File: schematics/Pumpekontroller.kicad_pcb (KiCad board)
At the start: 2 copper layers, 129.5 x 85.1 mm, 15 parts, among them Q1 BC548, Q2 BC548, SW1 SW_Push, SW2 SW_Push, U1 WeMos_D1_mini

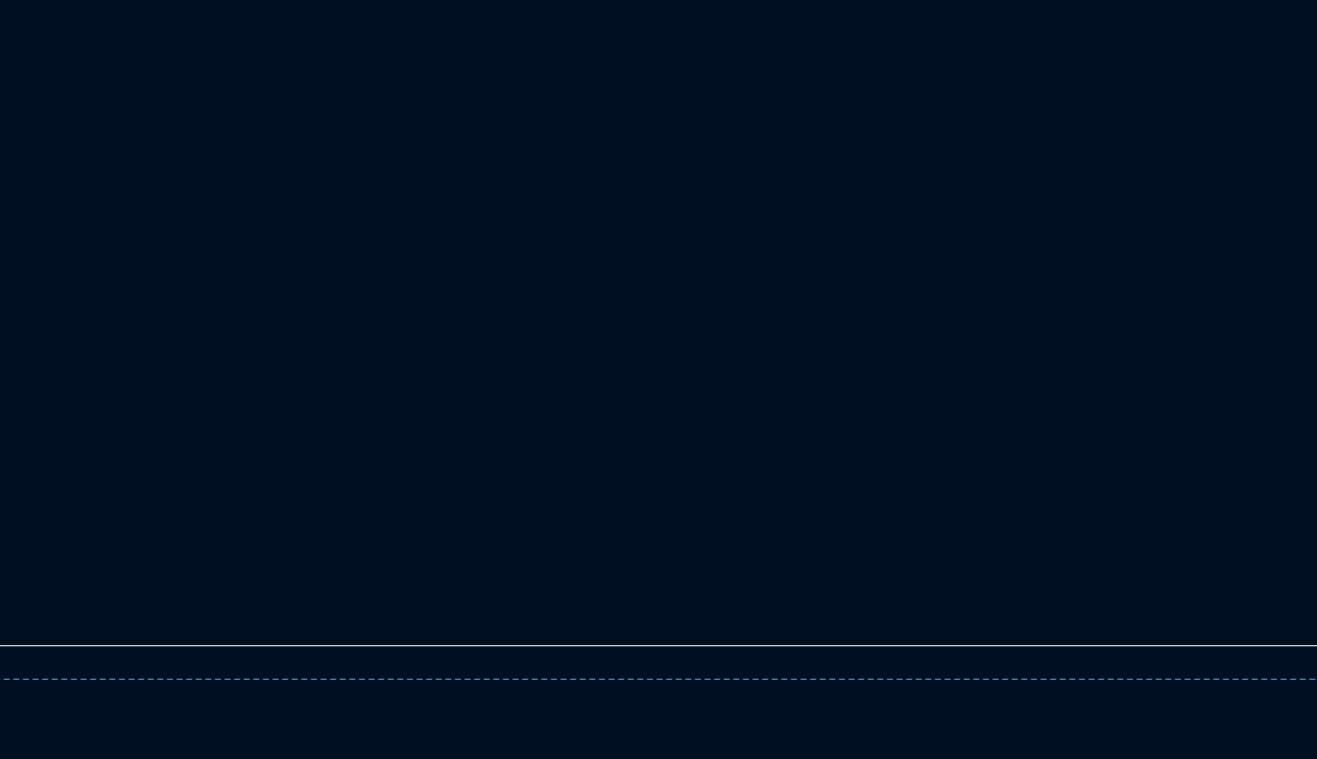
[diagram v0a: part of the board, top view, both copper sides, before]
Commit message: Update schematics with relay and pump circuit. Need more work.
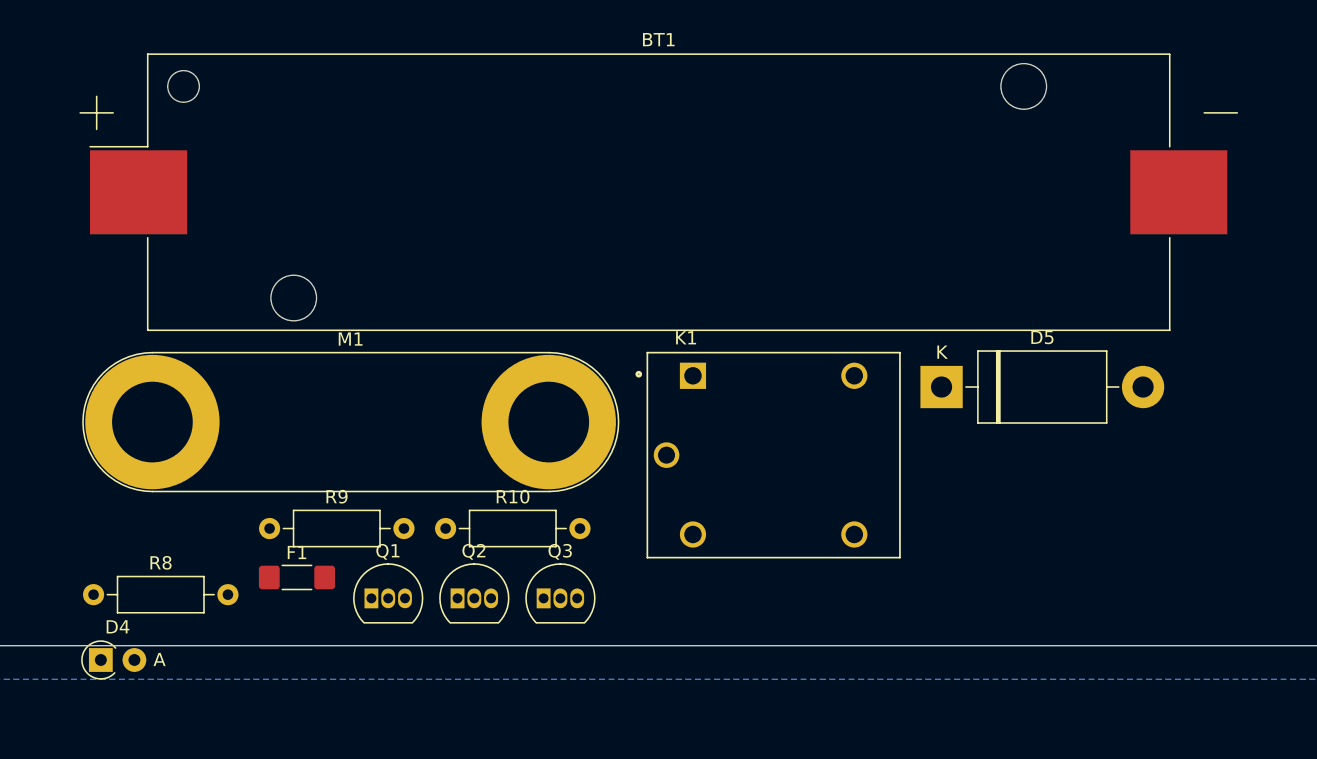
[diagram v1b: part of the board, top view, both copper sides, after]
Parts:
- added BT1: Battery 12V, Battery:BatteryHolder_Keystone_1042_1x18650, F.Cu at (149.9, 17.8)
- added D4: STPS3L60RL, Diode_THT:D_A-405_P2.54mm_Vertical_AnodeUp, F.Cu at (107.7, 53.1)
- added D5: LED, Diode_THT:D_DO-201AD_P15.24mm_Horizontal, F.Cu at (171.2, 32.5)
- added F1: Fuse, Fuse:Fuse_1806_4516Metric_Pad1.57x1.80mm_HandSolder, F.Cu at (122.5, 46.9)
- added K1: SRD-05VDC-SL-C, SRD-05VDC-SL-C:RELAY_SRD-05VDC-SL-C, F.Cu at (158.6, 37.7)
- added M1: Motor_DC, Connector:Banana_Jack_2Pin, F.Cu at (111.6, 35.2)
- added Q1: BC547, Package_TO_SOT_THT:TO-92_Inline, F.Cu at (128.1, 48.5)
- added Q2: BC547, Package_TO_SOT_THT:TO-92_Inline, F.Cu at (134.6, 48.5)
- added Q3: BC547, Package_TO_SOT_THT:TO-92_Inline, F.Cu at (141.2, 48.5)
- added R10: 2.2kΩ, Resistor_THT:R_Axial_DIN0207_L6.3mm_D2.5mm_P10.16mm_Horizontal, F.Cu at (133.7, 43.2)
- added R8: 1kΩ, Resistor_THT:R_Axial_DIN0207_L6.3mm_D2.5mm_P10.16mm_Horizontal, F.Cu at (107.1, 48.2)
- added R9: 1kΩ, Resistor_THT:R_Axial_DIN0207_L6.3mm_D2.5mm_P10.16mm_Horizontal, F.Cu at (120.4, 43.2)
- R2, R7: value R -> 100kΩ
- R3: value R -> 220Ω
- R4, R5: value R -> 100Ω
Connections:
- net GND renamed +5V
- R4 pad 1: Net-(R4-Pad1) -> Net-(Q1-Pad3)
- R5 pad 1: Net-(R5-Pad1) -> Net-(Q2-Pad3)
- U1 pad 4: Net-(R5-Pad1) -> Net-(U1-Pad4)
- U1 pad 5: Net-(R4-Pad1) -> Net-(U1-Pad5)

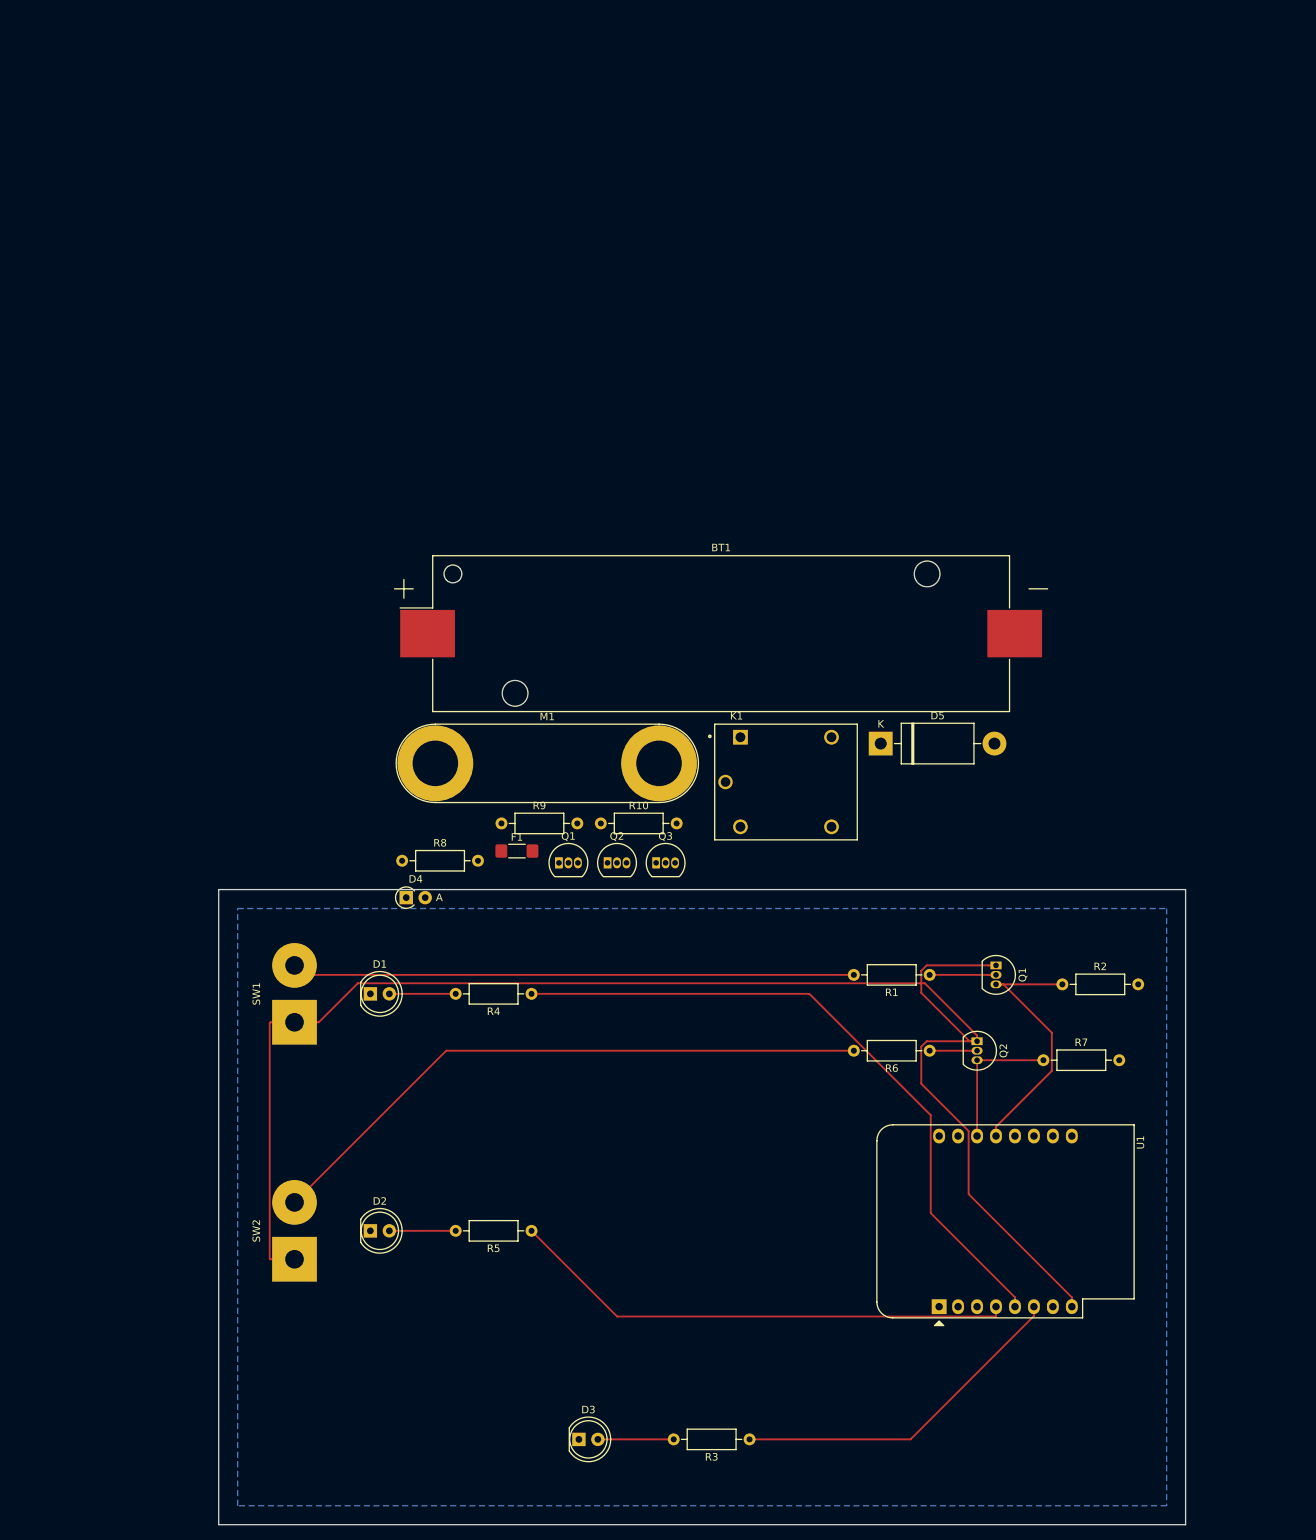
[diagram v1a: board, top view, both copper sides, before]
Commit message: Corrected LED-resistor sequence for water sensors. More coherent numbering of sensor components.
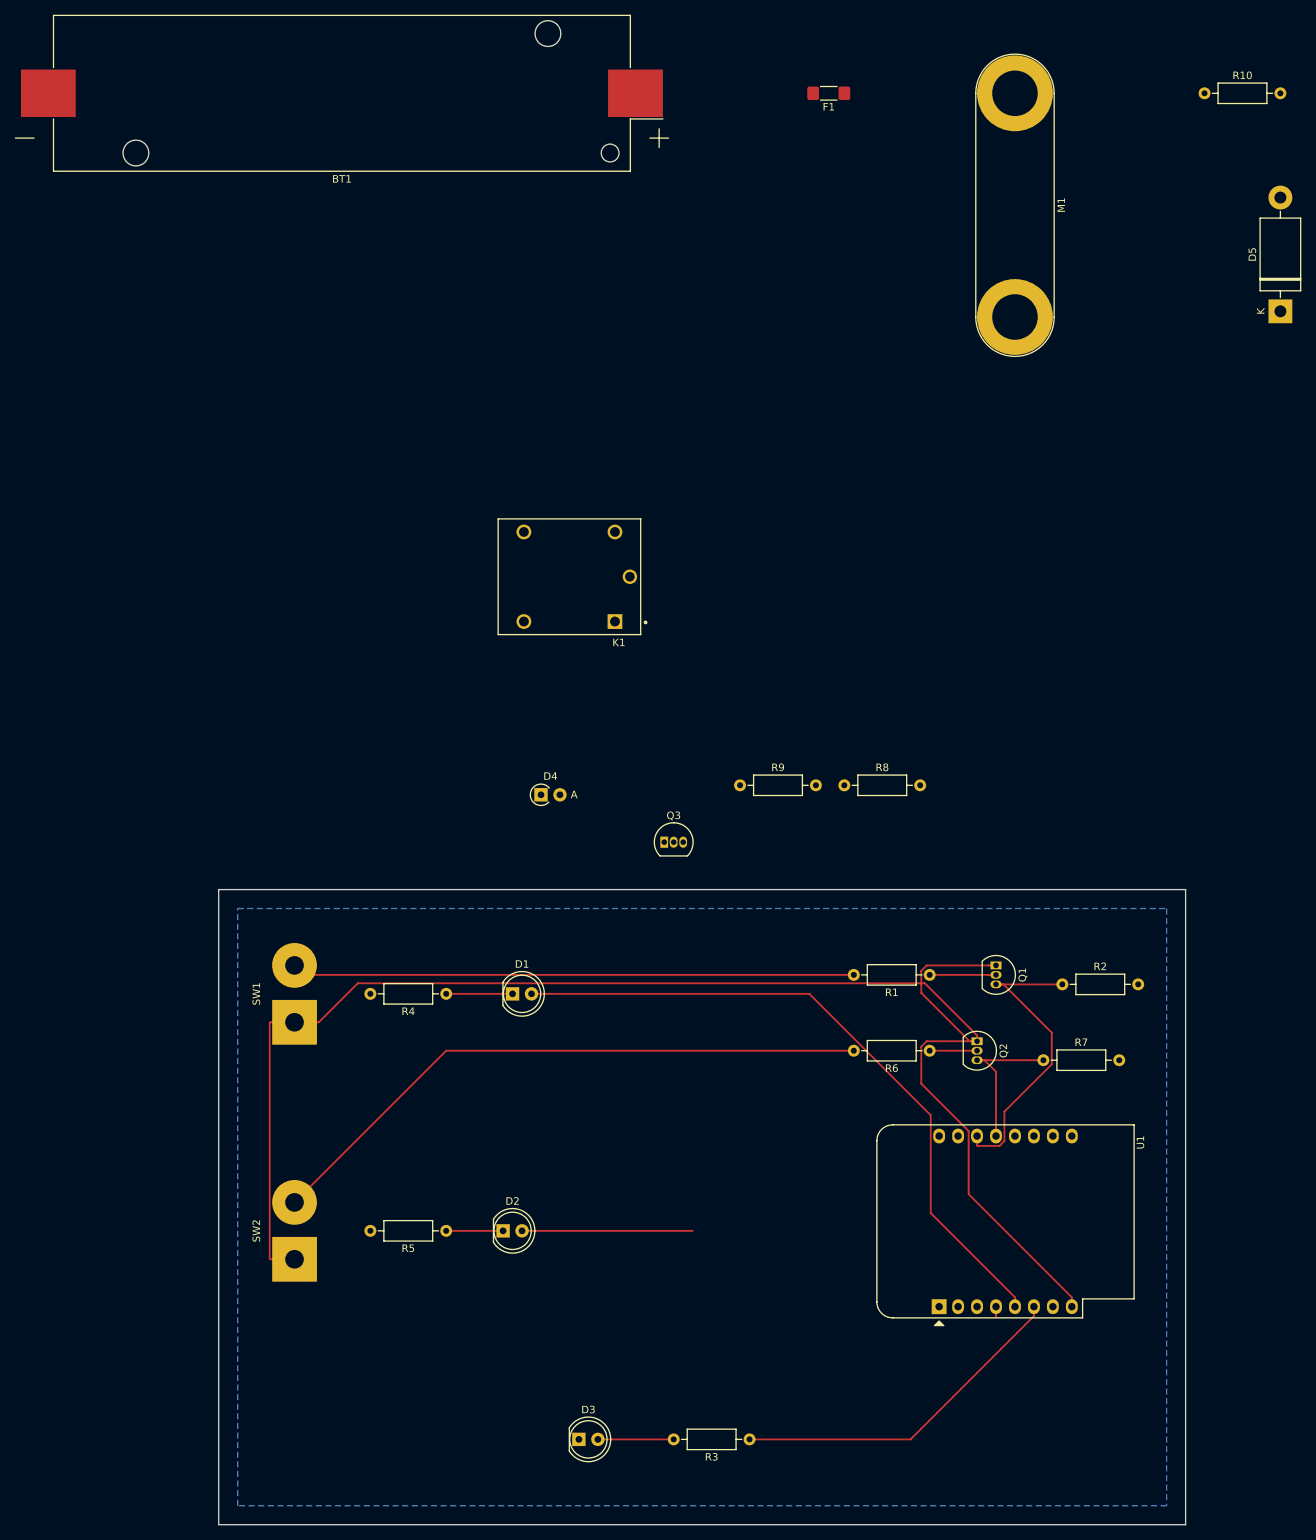
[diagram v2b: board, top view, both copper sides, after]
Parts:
- removed the Q1 at (128.1, 48.5)
- removed the Q2 at (134.6, 48.5)
- Q1, Q2: value BC548 -> BC547
- moved R10 126.9 mm to (214.6, -54.6)
- moved M1 118.7 mm to (189.2, -54.6), turned to 270 degrees
- moved F1 109.8 mm to (164.3, -54.6), turned to 180 degrees
- moved BT1 88.4 mm to (99.1, -54.6), turned to 180 degrees
- moved D5 78.9 mm to (224.8, -25.4), turned to 90 degrees
- moved R8 60.1 mm to (166.4, 38.1)
- moved K1 40.0 mm to (129.5, 10.2), turned to 180 degrees
- moved R9 32.4 mm to (152.4, 38.1)
- moved D4 22.7 mm to (125.7, 39.4)
- moved D1 19.0 mm to (121.9, 66.0)
- moved D2 17.8 mm to (120.7, 97.8)
- moved R4 11.4 mm to (113.0, 66.0)
- moved R5 11.4 mm to (113.0, 97.8)
- moved Q3 2.97 mm to (142.2, 45.7)
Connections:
- D1 pad 1: +5V -> Net-(D1-Pad1)
- D2 pad 1: +5V -> Net-(D2-Pad1)
- K1 pad NC: Net-(K1-PadNC) -> (no net)
- Q1 pad 3: Net-(Q1-Pad3) -> Net-(D1-Pad2)
- Q2 pad 3: Net-(Q2-Pad3) -> Net-(D2-Pad2)
- R2 pad 1: Net-(Q1-Pad3) -> Net-(D1-Pad2)
- R4 pad 1: Net-(Q1-Pad3) -> Net-(D1-Pad1)
- R4 pad 2: Net-(D1-Pad2) -> +5V
- R5 pad 1: Net-(Q2-Pad3) -> Net-(D2-Pad1)
- R5 pad 2: Net-(D2-Pad2) -> +5V
- R7 pad 1: Net-(Q2-Pad3) -> Net-(D2-Pad2)
- R8 pad 1: Net-(Q3-Pad2) -> Net-(R8-Pad1)
- R9 pad 1: Net-(R8-Pad2) -> Net-(Q3-Pad2)
- R9 pad 2: Net-(R9-Pad2) -> Net-(R8-Pad1)
- U1 pad 1: Net-(U1-Pad1) -> (no net)
- U1 pad 11: Net-(U1-Pad11) -> (no net)
- U1 pad 12: Net-(U1-Pad12) -> (no net)
- U1 pad 13: Net-(Q1-Pad3) -> Net-(D2-Pad2)
- U1 pad 14: Net-(Q2-Pad3) -> Net-(D1-Pad2)
- U1 pad 15: Net-(U1-Pad15) -> (no net)
- U1 pad 16: Net-(U1-Pad16) -> (no net)
- U1 pad 2: Net-(U1-Pad2) -> (no net)
- U1 pad 3: Net-(R9-Pad2) -> Net-(R8-Pad2)
- U1 pad 4: Net-(U1-Pad4) -> (no net)
- U1 pad 5: Net-(U1-Pad5) -> (no net)
- U1 pad 7: Net-(U1-Pad7) -> (no net)
- U1 pad 9: Net-(U1-Pad9) -> (no net)
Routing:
- net Net-(U1-Pad5): track 0.00 -> 90.5 mm
- net Net-(R4-Pad1): track 90.5 -> 0.00 mm
- net Net-(R5-Pad1): track 68.3 -> 0.00 mm
- net Net-(Q1-Pad3): track 36.0 -> 0.00 mm
- net Net-(D2-Pad2): track 8.89 -> 44.8 mm
- net Net-(D1-Pad2): track 8.89 -> 41.4 mm
- net Net-(Q2-Pad3): track 19.0 -> 0.00 mm
- net Net-(D1-Pad1): track 0.00 -> 8.89 mm
- net Net-(D2-Pad1): track 0.00 -> 7.62 mm
- net (no net): track 0.00 -> 1.36 mm
